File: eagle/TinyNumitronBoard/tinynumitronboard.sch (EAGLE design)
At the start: 25 parts, among them IC1 74LS595N, IC2 74LS595N

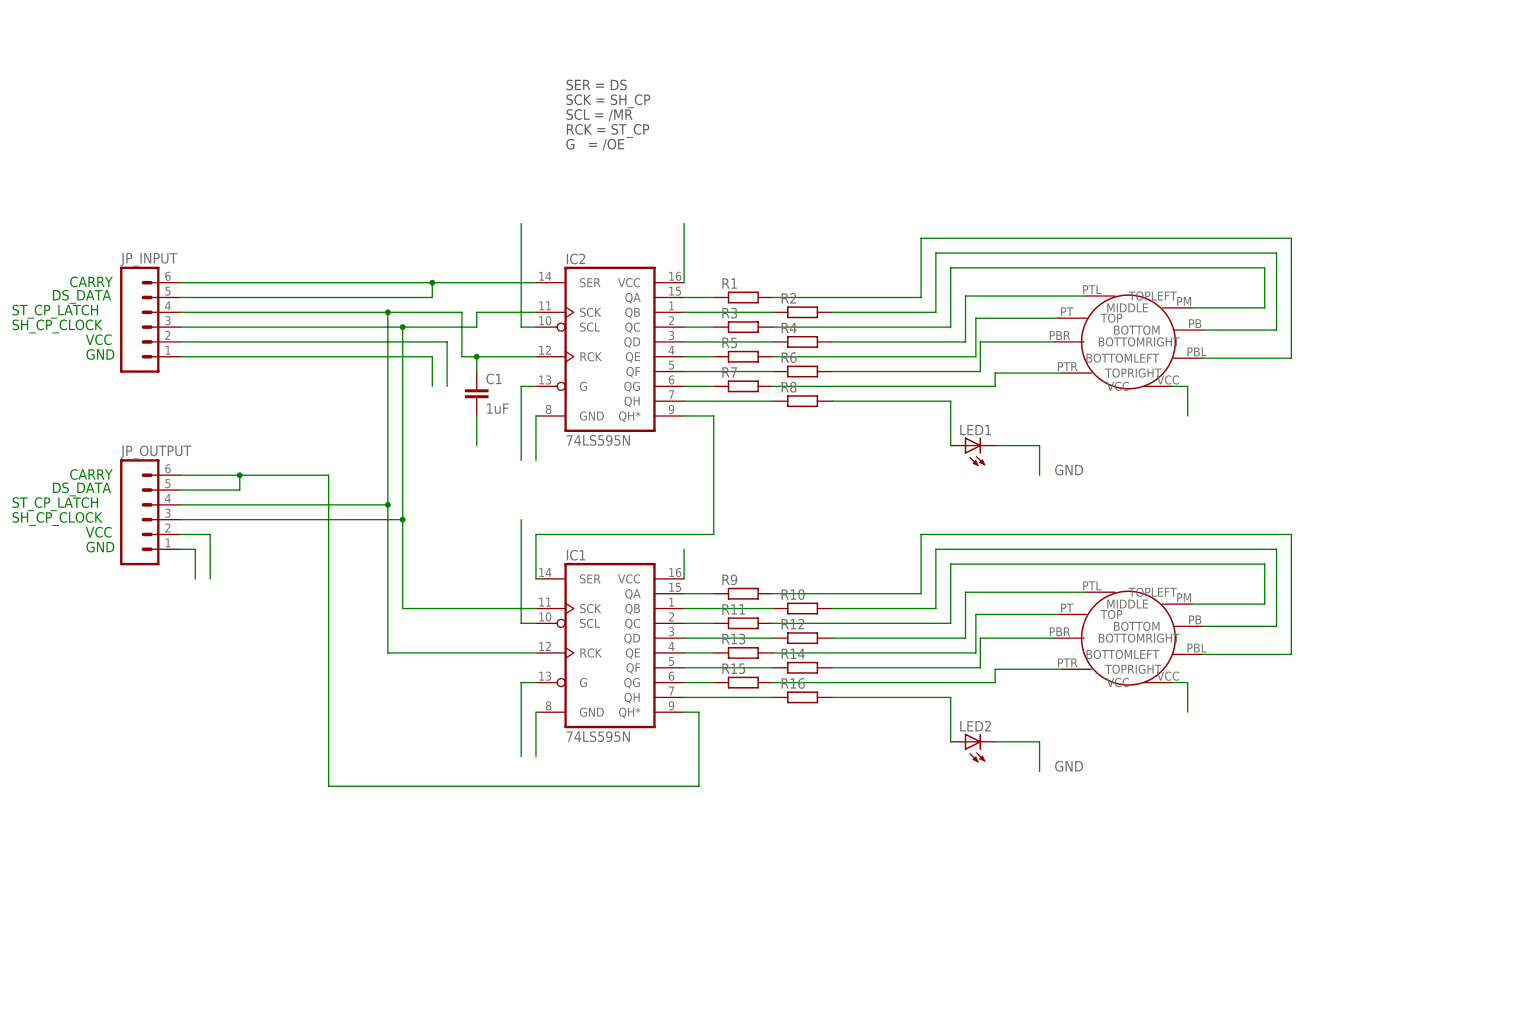
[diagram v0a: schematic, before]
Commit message: Dual version that accepts also SO16 version of 74595
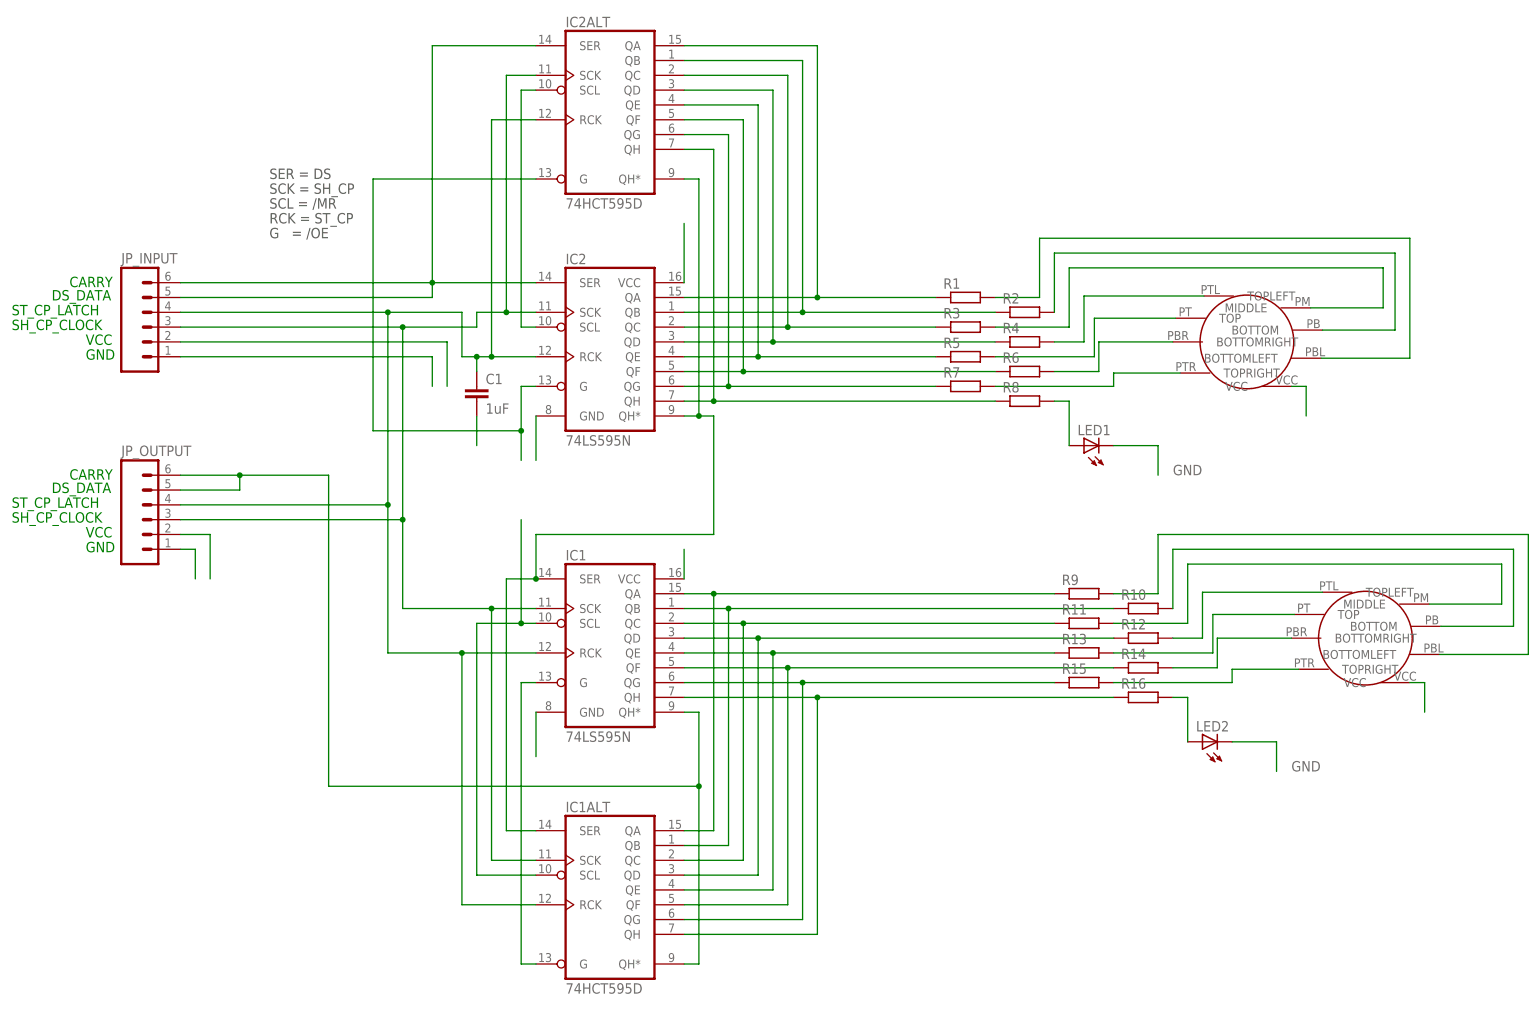
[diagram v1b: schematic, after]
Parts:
- added IC1ALT, IC2ALT: 74HCT595D, 74xx-eu:74HCT595D
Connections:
- removed net N$18: C1.1, IC1.RCK, IC2.RCK, JP_INPUT.4, JP_OUTPUT.4
- removed net N$29: IC1.QA, R9.1
- removed net N$30: IC1.QB, R10.1
- removed net N$31: IC1.QC, R11.1
- removed net N$32: IC1.QD, R12.1
- removed net N$33: IC1.QE, R13.1
- removed net N$34: IC1.QF, R14.1
- removed net N$35: IC1.QG, R15.1
- removed net N$36: IC1.QH, R16.1
- new net N$23: IC1.SER, IC1ALTA.SER, IC2.QH*, IC2ALTA.QH*
- new net N$39: IC2.QB, IC2ALTA.QB, R2.1
- new net N$41: IC2.QA, IC2ALTA.QA, R1.1
- new net N$42: IC2.QG, IC2ALTA.QG, R7.1
- new net N$43: IC2.QF, IC2ALTA.QF, R6.1
- new net N$48: C1.1, IC1.RCK, IC1ALTA.RCK, IC2.RCK, IC2ALTA.RCK, JP_INPUT.4, JP_OUTPUT.4
- new net N$52: IC1.QA, IC1ALTA.QA, R9.1
- new net N$54: IC1.SCK, IC1ALTA.SCK, IC2.SCK, IC2ALTA.SCK, JP_INPUT.3, JP_OUTPUT.3
- new net N$56: IC1.QH*, IC1ALTA.QH*, JP_OUTPUT.5, JP_OUTPUT.6
- net GND: now also IC1ALTA.G, IC2ALTA.G
- net N$10: now also IC1.QD, IC1ALTA.QD, R12.1; no longer IC2.QC, R3.1
- net N$11: now also IC1.QE, IC1ALTA.QE, R13.1; no longer IC2.QD, R4.1
- net N$12: now also IC2ALTA.QE
- net N$13: now also IC2.QD, IC2ALTA.QD, R4.1; no longer IC2.QF, R6.1
- net N$14: now also IC1.QF, IC1ALTA.QF, R14.1; no longer IC2.QG, R7.1
- net N$15: now also IC1.QG, IC1ALTA.QG, R15.1; no longer IC2.SER, JP_INPUT.5, JP_INPUT.6
- net N$16: now also IC2ALTA.QH
- net N$19: now also IC2.QC, IC2ALTA.QC, R3.1; no longer IC1.SCK, IC2.SCK, JP_INPUT.3, JP_OUTPUT.3
- net N$22: now also IC1.QH, IC1ALTA.QH, R16.1; no longer IC1.QH*, JP_OUTPUT.5, JP_OUTPUT.6
- net N$38: now also IC2.SER, IC2ALTA.SER, JP_INPUT.5, JP_INPUT.6; no longer IC1.SER, IC2.QH*
- net N$8: now also IC1.QB, IC1ALTA.QB, R10.1; no longer IC2.QA, R1.1
- net N$9: now also IC1.QC, IC1ALTA.QC, R11.1; no longer IC2.QB, R2.1
- net VCC: now also IC1ALTA.SCL, IC2ALTA.SCL
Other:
- moved on the sheet: LED1, LED2, R1, R10, R11, R12, R13, R14, R15, R16, R2, R3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
